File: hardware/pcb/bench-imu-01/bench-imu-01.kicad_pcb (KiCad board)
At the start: 4 copper layers, 150 x 95 mm, 53 parts, among them J1 USB_C_Receptacle_GCT_USB4105-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, J2 PinHeader_1x04_P2.54mm_Vertic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, J3 PinHeader_1x04_P2.54mm_Vertic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, J4 BarrelJack_CUI_PJ-102AH_Horiz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, M1 TerminalBlock_MaiXu_MX126-5.0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, SW1 SW_PUSH_6mm, U1 LQFP-32_7x7mm_P0.8mm, U2 Bosch_LGA-14_3x2.5mm_P0.5mm, U3 SOT-23-5, U4 SOT-23-6, U5 HTSSOP-24-1EP_4.4x7.8mm_P0.65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, U6 HTSSOP-20-1EP_4.4x6.5mm_P0.65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

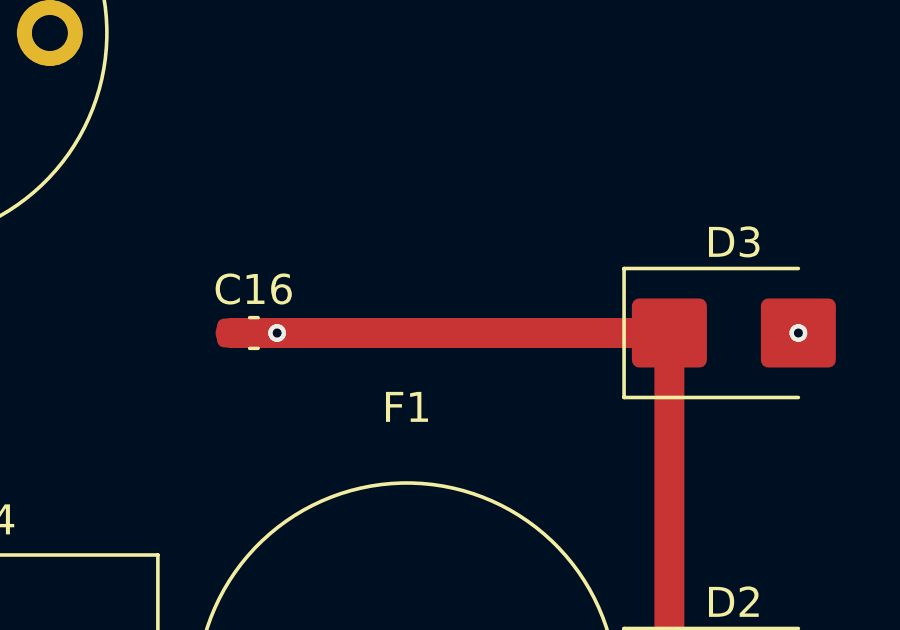
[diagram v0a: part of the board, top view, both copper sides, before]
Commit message: ISS-036: whole-board-aware reroute fixes (4 of 4 targeted, 3 of 4 closed)
Per Kyosuke's explicit go-ahead to build real whole-board-aware routing
capability (not deferred), rather than the single-obstacle-only detour
that was tried and reverted last round.

Built a whole-board-aware collision checker using pcbnew's own
SHAPE.Collide/SEG.Collide geometry primitives (KiCad's own DRC engine,
not a hand-rolled approximation) that checks every candidate reroute path
against the board's ENTIRE other-net copper set before accepting it.

Of the 4 named via_vs_inner_layer_copper targets from the prior triage:
- 3 J1-area instances (GND through-via vs VBUS_5V In2.Cu track): fixed,
  whole-board-clear detours found and verified.
- 1 U5-area instance (I2C1_SDA via vs I2C1_SCL track): confirmed
  genuinely intractable via direct geometric measurement -- the two vias
  sit at U5's own 0.65mm pin pitch with only 0.05mm physical gap between
  copper edges, below any usable clearance regardless of technique.

Also found 1 additional outer-layer fix (VM_MOTOR near J4) via an
automated batch search; 4 further iterations found 0 more tractable
fixes -- a genuine plateau (not a search-parameter limit), confirming
the remaining ~54 outer-layer violations are the already-disclosed
autorouter/fine-pitch-proximity-class gap (14 confirmed within 8mm of
U5/U6 via direct geometric check). Did not attempt a U5/U6 placement
change this round: U5's placement was already the subject of ISS-031's
own thermal-via fix, and shifting it risks reopening that fix without a
wider verification budget than this round allows.

All 4 fixes integrated into generate_pcb.py via a new REROUTE_OVERRIDE
list + _apply_reroute_overrides() (matches by net+position, not
UUID/object identity, since every script re-run creates fresh objects;
loud warning + skip, never silent no-op or partial apply, if a source
segment goes stale).

Verified via real, repeated DRC (3 fresh kicad-cli pcb drc runs before
vs. after): shortin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
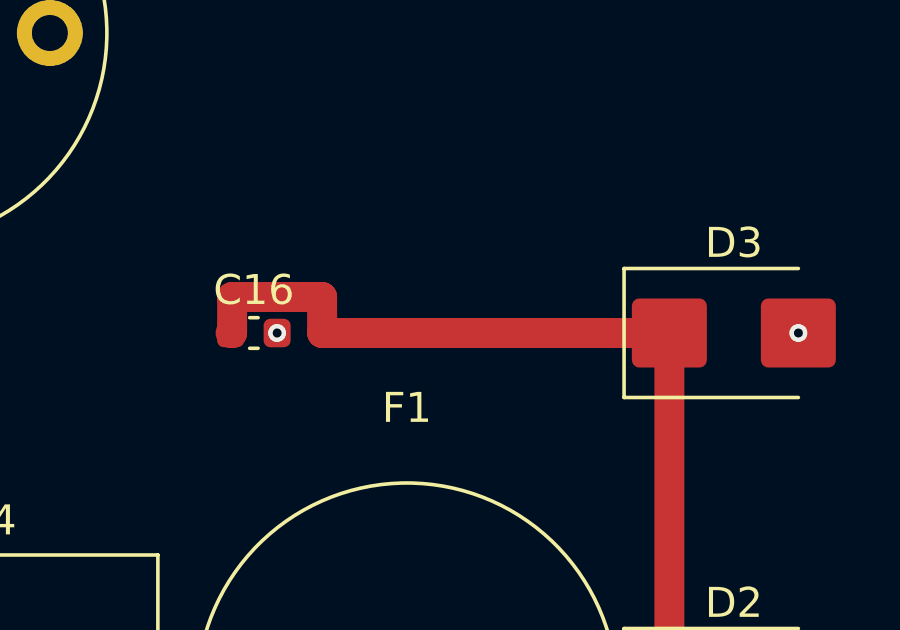
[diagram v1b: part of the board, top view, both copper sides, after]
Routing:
- net VM_MOTOR: track 76.7 -> 79.1 mm
- net VBUS_5V: track 62.7 -> 63.7 mm

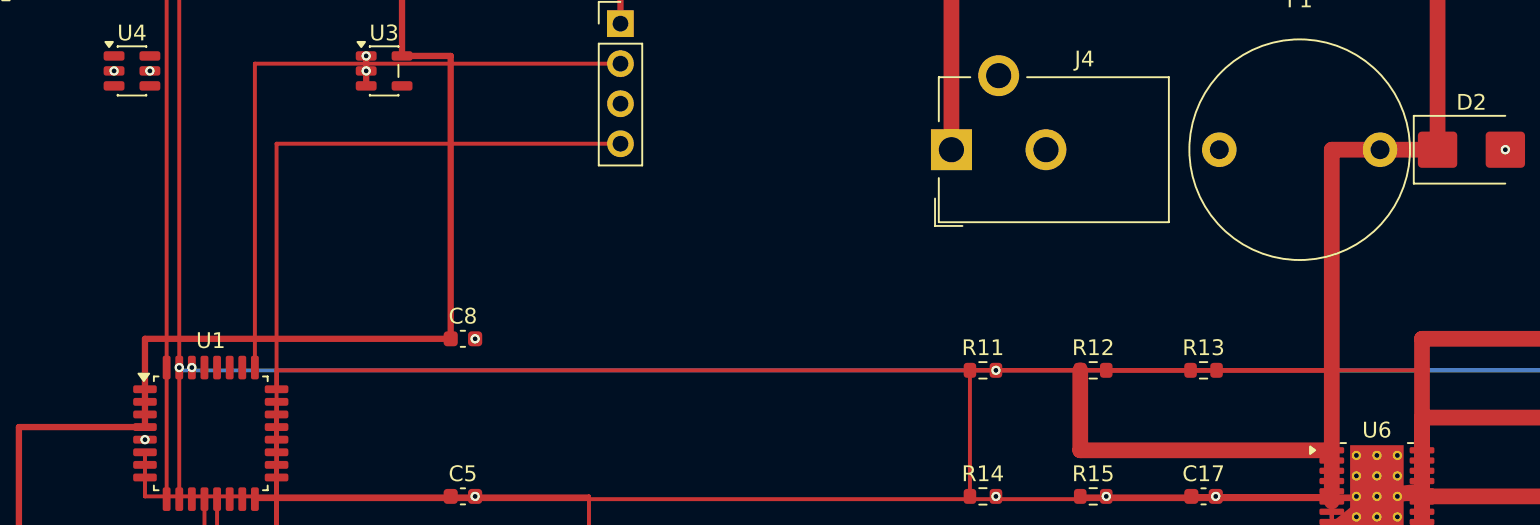
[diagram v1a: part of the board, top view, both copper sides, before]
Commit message: ISS-036: solder_mask_bridge sweep -- 2 more whole-board-aware fixes
Per explicit request to keep pushing on ISS-036 rather than stopping at
the prior round's natural checkpoint, ran a new whole-board-aware
detour search against solder_mask_bridge -- the largest untriaged DRC
category (209-226 instances across runs, dwarfing shorting_items'
49-58), never previously deep-dived.

Root-cause analysis first: 209/211 instances are track-vs-pad conflicts
(a different-net track passing close enough to an unrelated pad that
their solder-mask apertures merge into one shared opening -- a real
solder-bridging risk if fabricated as-is, not a cosmetic DRC nag).
59% (125/211) fall within 15mm of U5/U6, matching the already-documented
fine-pitch-package-proximity pattern; the remaining 41% (86/211) are
spread across the rest of the board -- confirming this is NOT purely a
U5/U6 placement problem (a placement shift could, at best, address
roughly half the category) but a genuine limitation of the MST+L-bend
router's lack of channel/congestion awareness in a densely-routed
board, consistent with (and reinforcing) the same conclusion already
reached for the outer-layer shorting_items category.

Uniquely identified the specific track object for 206/211 violations
(net+position+length matching, 3 skipped as ambiguous) and ran the
same validated whole-board-aware collision search (pcbnew's own
SHAPE.Collide/SEG.Collide, checking each candidate detour against the
board's ENTIRE other-net copper) against all 206: found genuinely
tractable fixes for only 2 unique track objects (~1% yield) -- one on
3V3 (flagged against 3 different nearby pads simultaneously, all
resolved by the one fix) and one on VM_MOTOR. This closely matches the
~2% yield already found for the ~54-item outer-layer shorting_items
sweep in the prior round, now confirmed via a second, independent,
large-scale (206-item) test -- strong, reproducible evidence that local
single-track detour search has genuinely hit its ceiling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
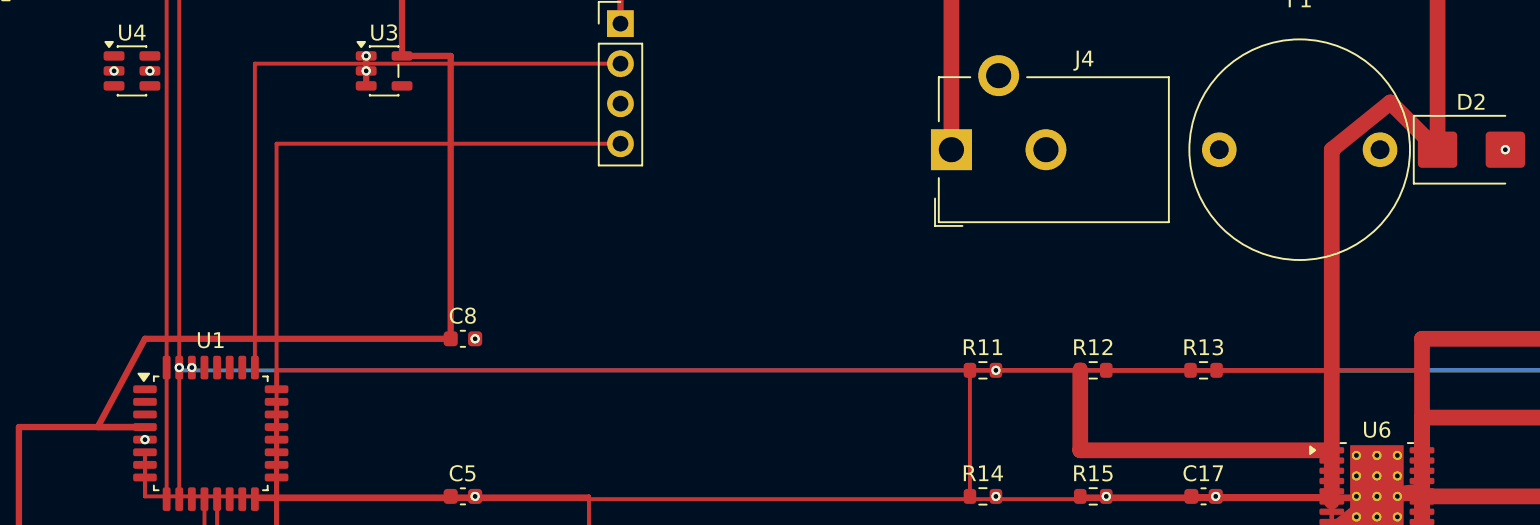
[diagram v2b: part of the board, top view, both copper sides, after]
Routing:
- net 3V3: track 175.0 -> 178.7 mm
- net VM_MOTOR: track 79.1 -> 81.4 mm
